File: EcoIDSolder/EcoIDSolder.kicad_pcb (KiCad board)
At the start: 2 copper layers, 15 x 37 mm, 9 parts, among them J1 Conn_02x08_Counter_Clockwise

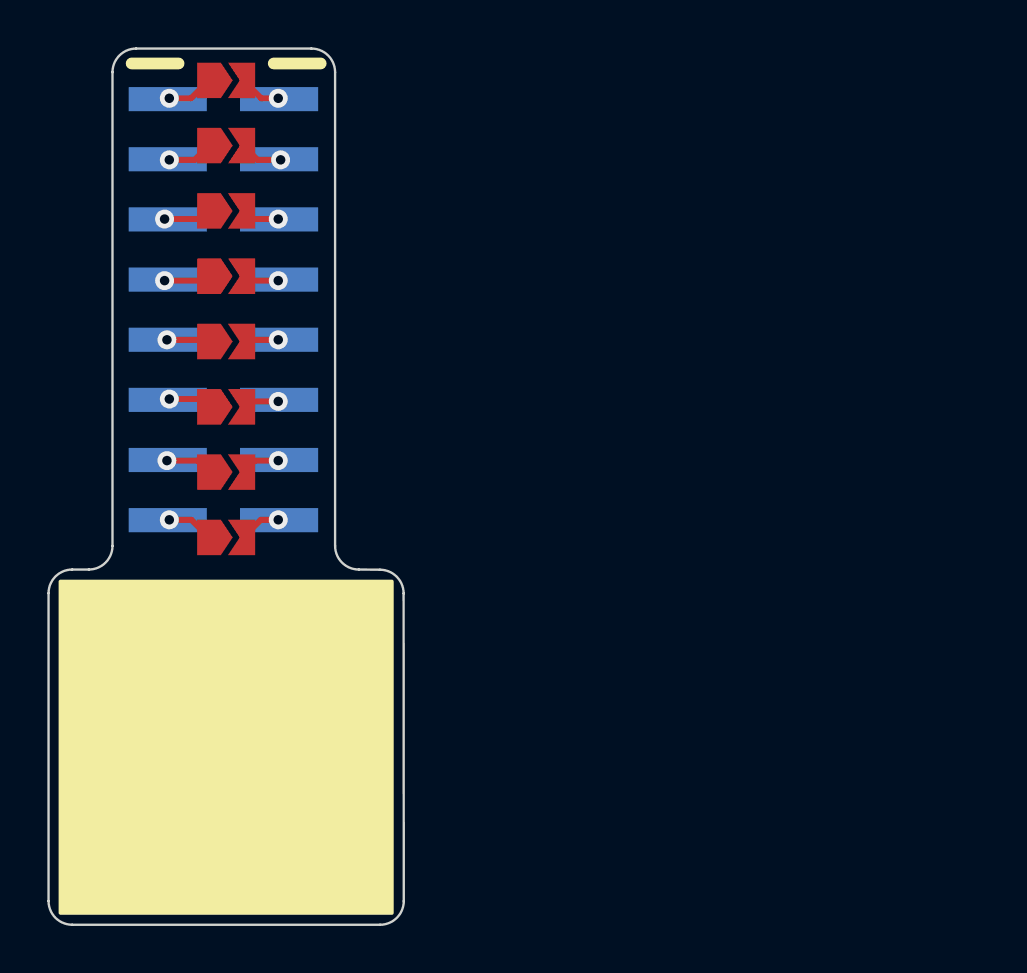
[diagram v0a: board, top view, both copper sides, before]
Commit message: Refactor solder PCB to same dimensions as switch PCB
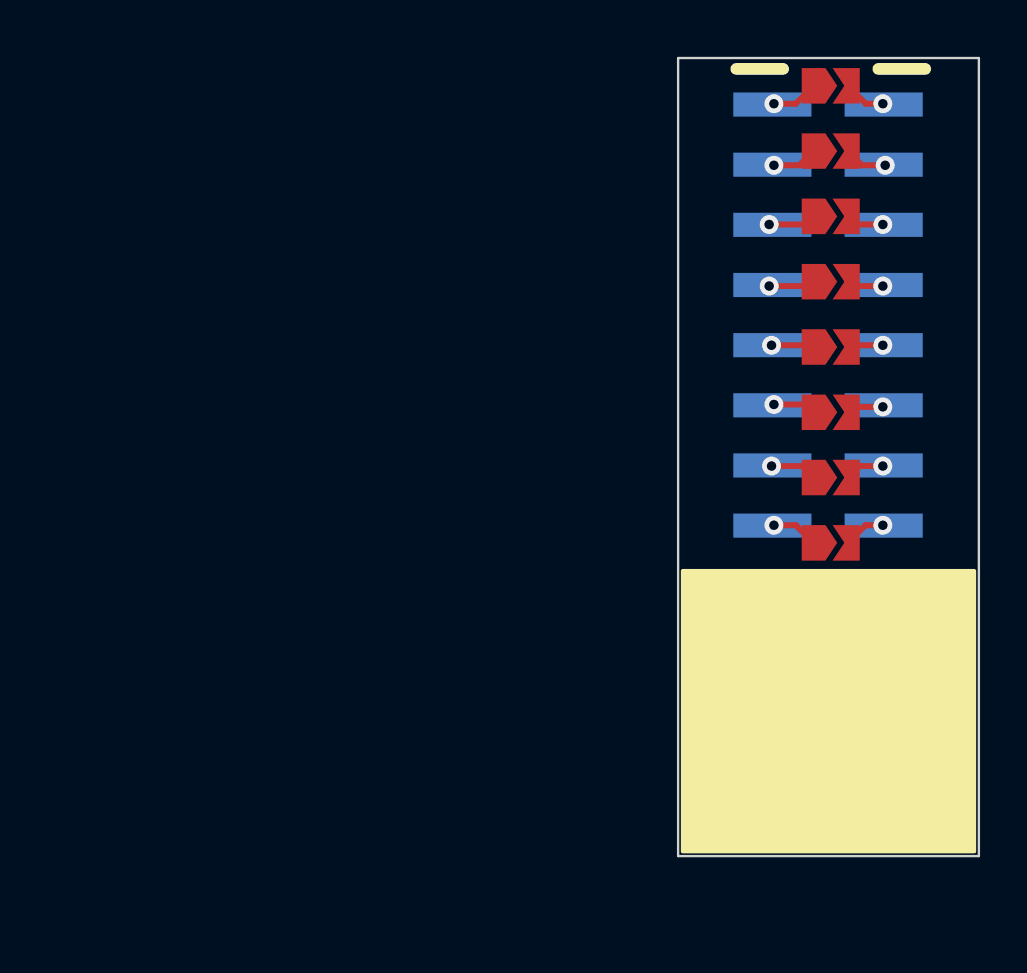
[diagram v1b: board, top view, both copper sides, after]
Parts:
- moved J1 25.5 mm to (173.2, 81.1)
- moved JP1 25.5 mm to (173.3, 71.4)
- moved JP2 25.5 mm to (173.3, 74.1)
- moved JP3 25.5 mm to (173.3, 76.9)
- moved JP4 25.5 mm to (173.3, 79.6)
- moved JP5 25.5 mm to (173.3, 82.4)
- moved JP6 25.5 mm to (173.3, 85.2)
- moved JP7 25.5 mm to (173.3, 87.9)
- moved JP8 25.5 mm to (173.3, 90.7)
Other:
- board size 15 x 37 mm -> 12.7 x 33.7 mm
- board text added: "BBC EcoID Solder v0.2"
- board text removed: "BBC EcoID Solder v0.1"
